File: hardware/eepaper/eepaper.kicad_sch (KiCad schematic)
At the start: 62 parts, among them J1 S2B-PH-SM4-TB, J2 USB4105-GF-A, J3 105162-0001, J4 FFC2B28-24-G, J5 Conn_01x19, Q1 SI2305-TP, Q2 PJC7400_R1_00001, U1 MCP73831-2-OT, U2 RT9080-33GJ5, U3 ESP32-C3-WROOM-02-H4

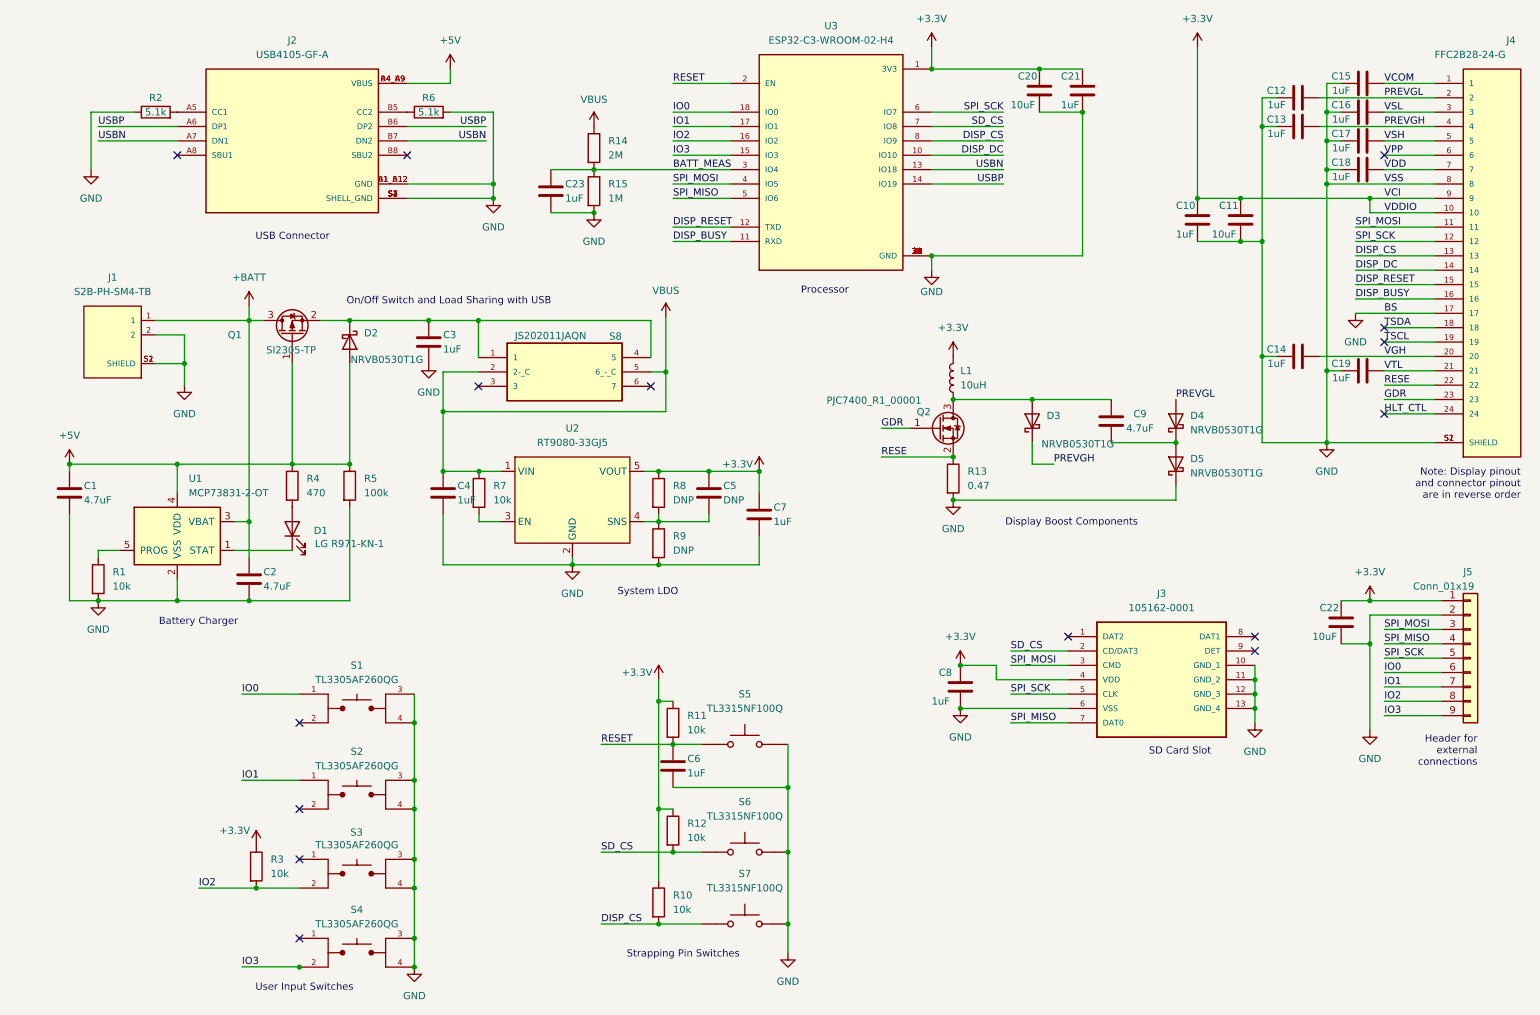
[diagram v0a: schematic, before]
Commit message: Add v2 hardware files sent to fabrication
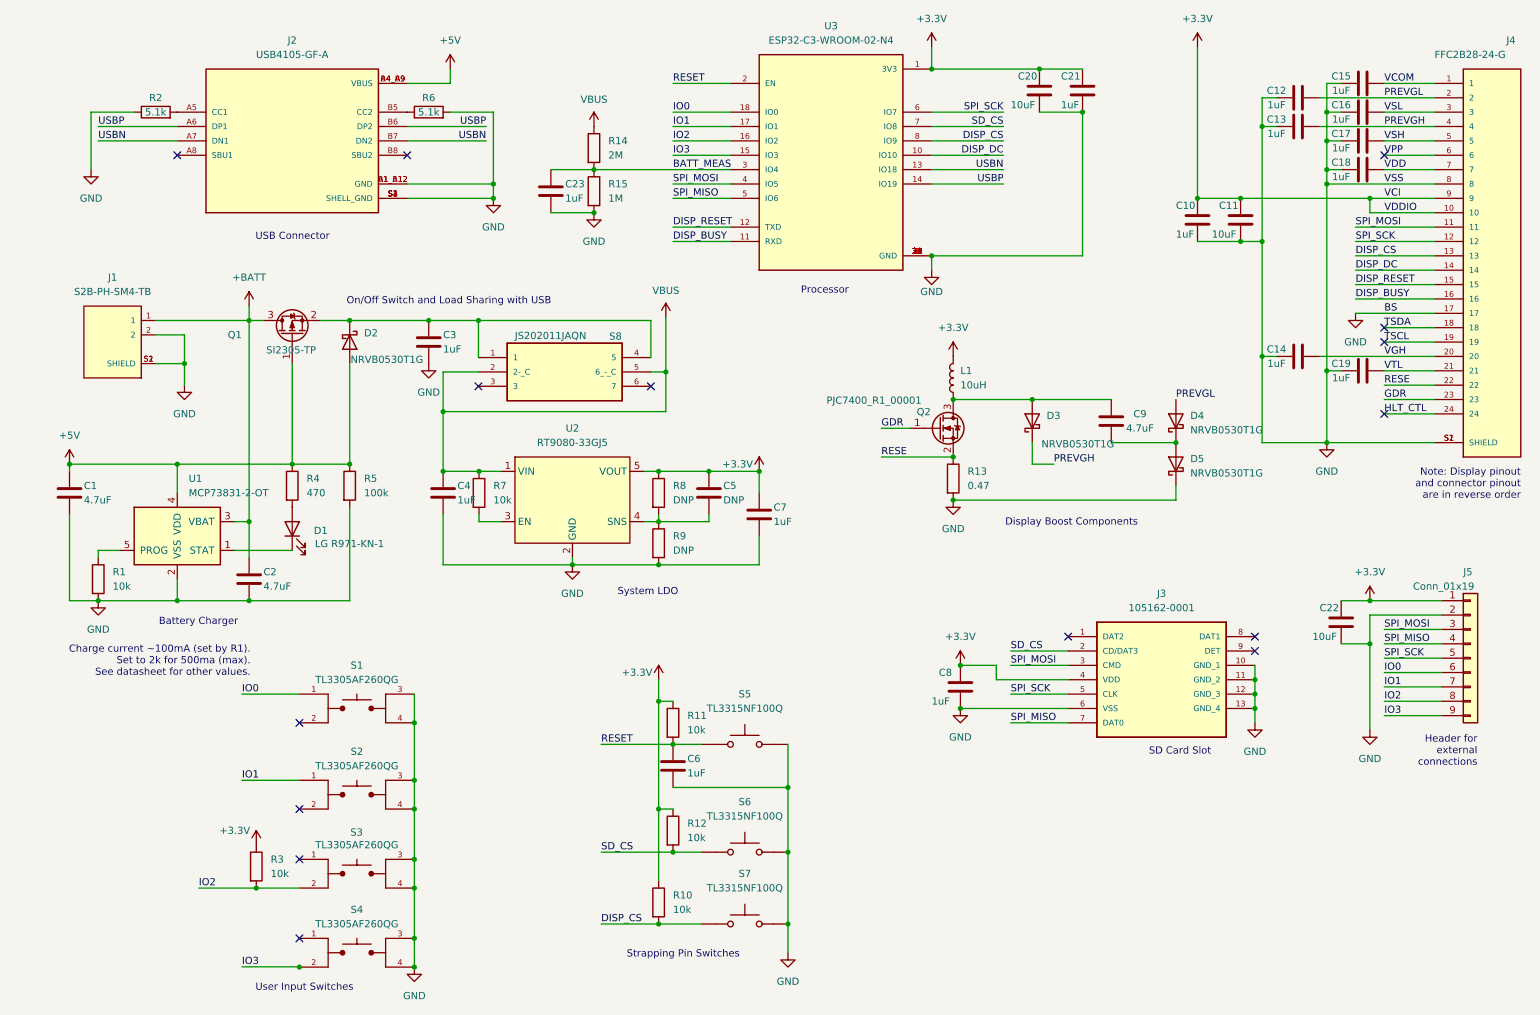
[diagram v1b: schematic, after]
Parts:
- U3: value ESP32-C3-WROOM-02-H4 -> ESP32-C3-WROOM-02-N4
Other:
- note added: "Charge current ~100mA (set by R1). Set to 2k for 500ma (max). See datasheet for other values."
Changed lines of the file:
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@@
+    (effects (font (size 1.27 1.27)) (justify right bottom))
+  )
+  (text "Charge current ~100mA (set by R1).\nSet to 2k for 500ma (max).\nSee datasheet for other values."
+    (at 53.594 135.4328 0)
     (effects (font (size 1.27 1.27)) (justify right bottom))
   )
@@
     (in_bom yes) (on_board yes) (fields_autoplaced)
     (property "Reference" "U3" (id 0) (at 156.21 20.32 0))
-    (property "Value" "ESP32-C3-WROOM-02-H4" (id 1) (at 156.21 22.86 0))
+    (property "Value" "ESP32-C3-WROOM-02-N4" (id 1) (at 156.21 22.86 0))
     (property "Footprint" "Project Footprints:MODULE_ESP32-C3-WROOM-02-H4" (id 2) (at 156.21 45.72 0)
       (effects (font (size 1.27 1.27)) (justify left bottom) hide)
@@
     )
     (path "/082b6270-54ea-45b5-8193-fd08dfeabc80"
-      (reference "U3") (unit 1) (value "ESP32-C3-WROOM-02-H4") (footprint "Project Footprints:MODULE_ESP32-C3-WROOM-02-H4")
-    )
-  )
+      (reference "U3") (unit 1) (value "ESP32-C3-WROOM-02-N4") (footprint "Project Footprints:MODULE_ESP32-C3-WROOM-02-H4")
+    )
+  )
